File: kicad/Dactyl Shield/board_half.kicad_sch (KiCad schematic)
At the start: 47 parts, among them J201 JST, J202 Split, J203 Column, J205 Foot, J206 Row, J207 Display, J208 Vic, J209 ResA, J210 Thumb_row, J211 Thumb_upper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

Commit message: fix: resistors have correct PCBA part id
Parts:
- R202, R205, R206: LCSC Part C23025 -> C17634
- R204: LCSC Part C23025 -> C25804
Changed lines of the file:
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@@
 	(title_block
 		(title "Hillside Dactyl Shield")
-		(date "2025-04-13")
+		(date "2025-04-19")
 		(rev "0.1.0-alpha.3")
 		(comment 1 "  Headers: MCU, key matrix and display")
@@
 			)
 		)
-		(property "LCSC Part" "C23025"
+		(property "LCSC Part" "C17634"
 			(at 148.59 130.81 0)
 			(effects
@@
 			)
 		)
-		(property "LCSC Part" "C23025"
+		(property "LCSC Part" "C17634"
 			(at 148.59 125.73 0)
 			(effects
@@
 			)
 		)
-		(property "LCSC Part" "C23025"
+		(property "LCSC Part" "C17634"
 			(at 148.59 135.89 0)
 			(effects
@@
 			)
 		)
-		(property "LCSC Part" "C23025"
+		(property "LCSC Part" "C25804"
 			(at 129.54 151.13 0)
 			(effects

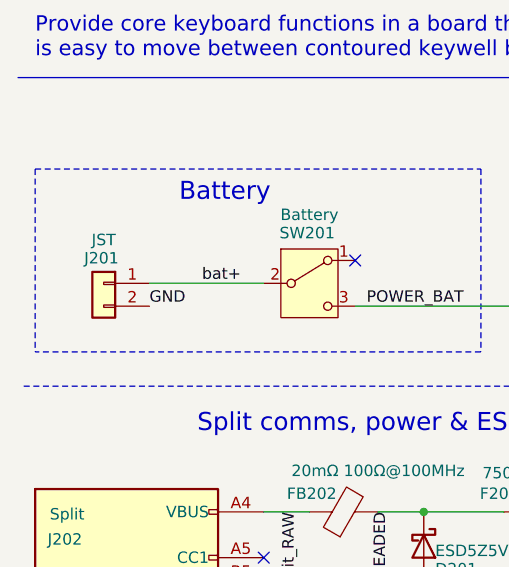
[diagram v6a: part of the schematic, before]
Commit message: feat(pcba): add JST-PH battery connector
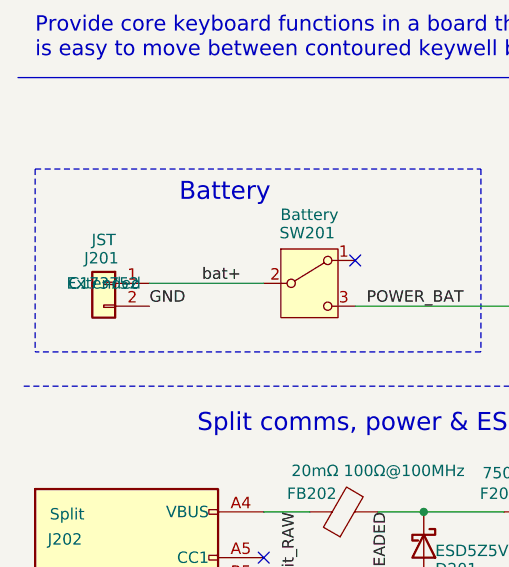
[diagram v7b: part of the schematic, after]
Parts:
- J201: Config DNF -> (none); JLC PCBA Type (none) -> Extended; LCSC Part (none) -> C173752
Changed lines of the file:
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@@
 			)
 		)
-		(property "Config" "DNF"
+		(property "Config" ""
 			(at 21.59 48.26 0)
 			(effects
@@
 			)
 		)
+		(property "JLC PCBA Type" "Extended"
+			(at 21.59 48.26 0)
+			(effects
+				(font
+					(size 1.27 1.27)
+				)
+			)
+		)
+		(property "LCSC Part" "C173752"
+			(at 21.59 48.26 0)
+			(effects
+				(font
+					(size 1.27 1.27)
+				)
+			)
+		)

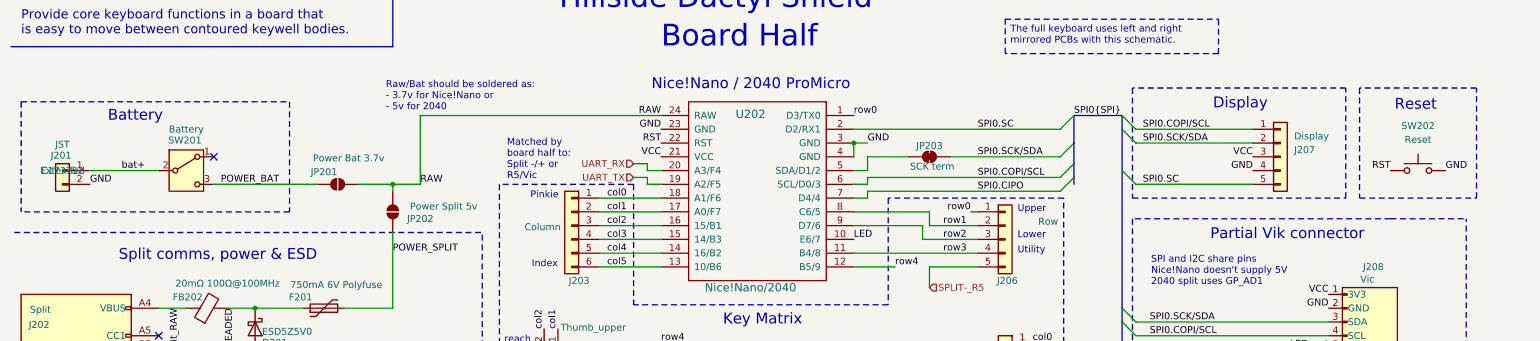
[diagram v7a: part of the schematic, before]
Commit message: feat(pcba): add reset switch
project exclusions exclude four way junction
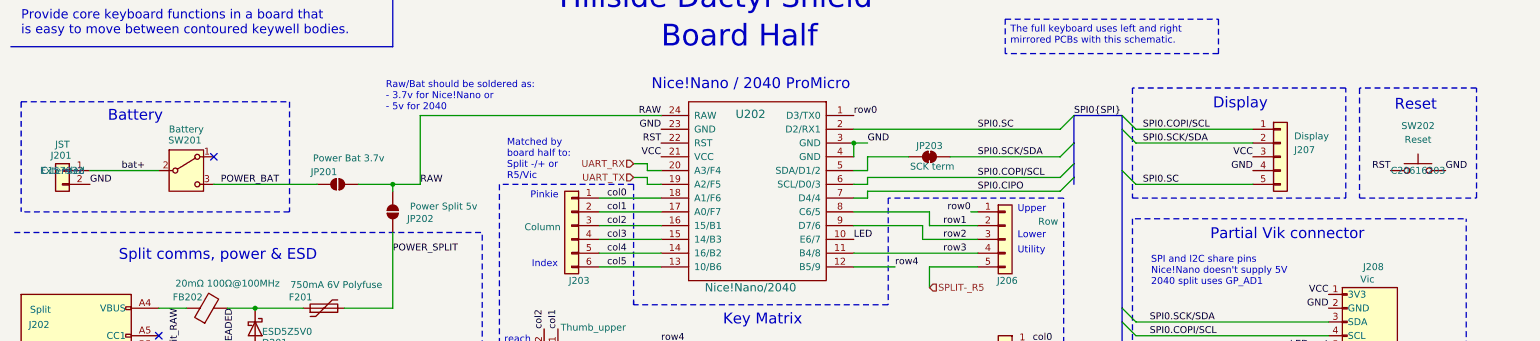
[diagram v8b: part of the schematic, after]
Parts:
- J201: LCSC Part C173752 -> C157932
- SW202: LCSC Part (none) -> C20616203
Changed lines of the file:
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@@
 			)
 		)
-		(property "LCSC Part" "C173752"
+		(property "LCSC Part" "C157932"
 			(at 21.59 48.26 0)
 			(effects
@@
 			)
 		)
+		(property "LCSC Part" "C20616203"
+			(at 271.78 48.26 0)
+			(effects
+				(font
+					(size 1.27 1.27)
+				)
+			)
+		)
